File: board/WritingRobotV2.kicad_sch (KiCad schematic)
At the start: 19 parts, among them J1 POWER-INPUT, J2 MOTOR-1-OUTPUT, J3 MOTOR-2-OUTPUT, J4 CAN-INPUT, U1 L7805, U2 MCP2551-I-P

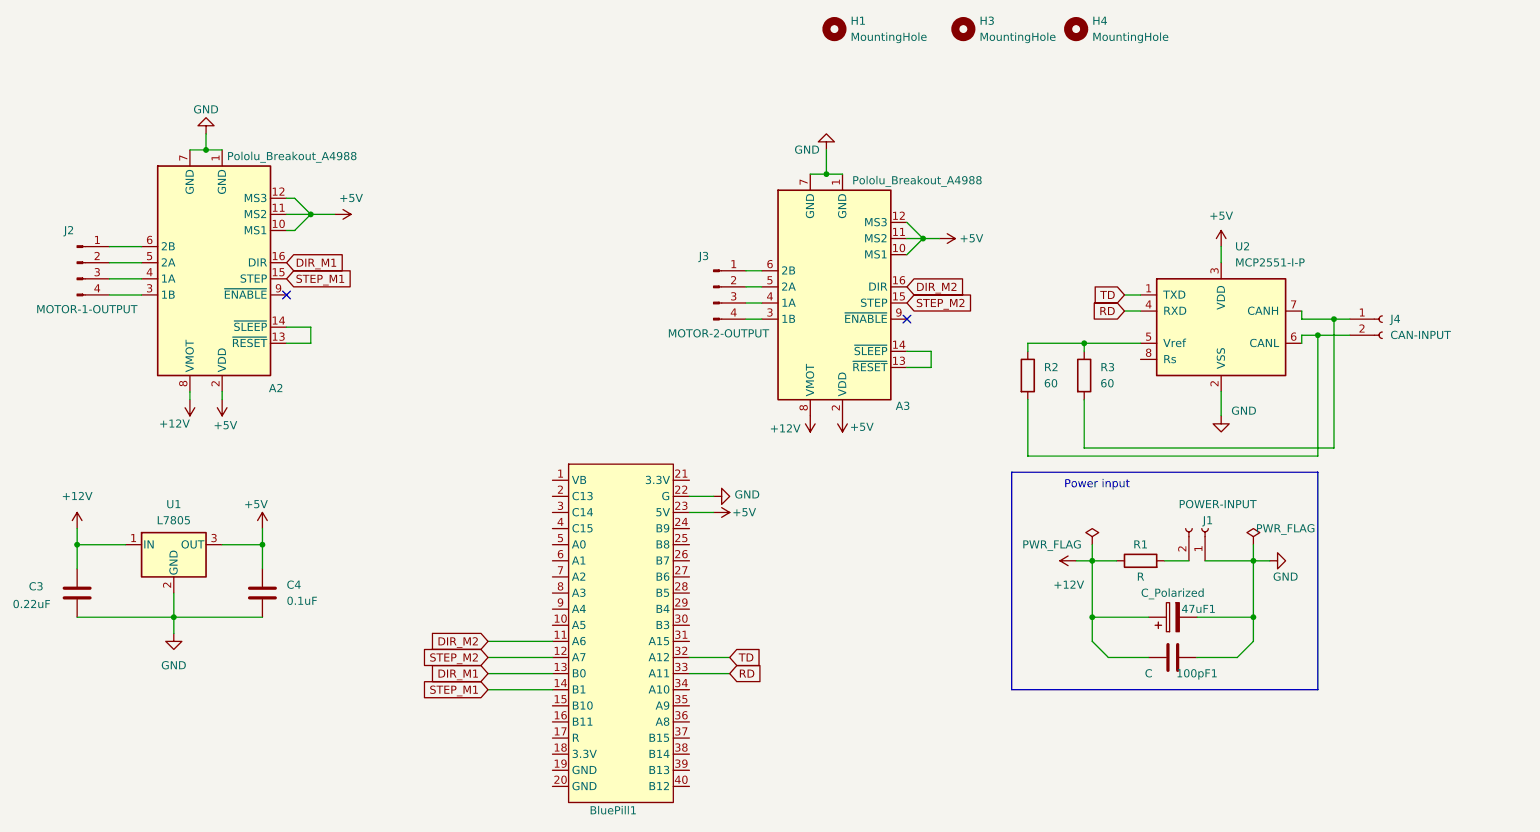
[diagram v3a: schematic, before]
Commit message: Board updated to STM32
Other files in rework
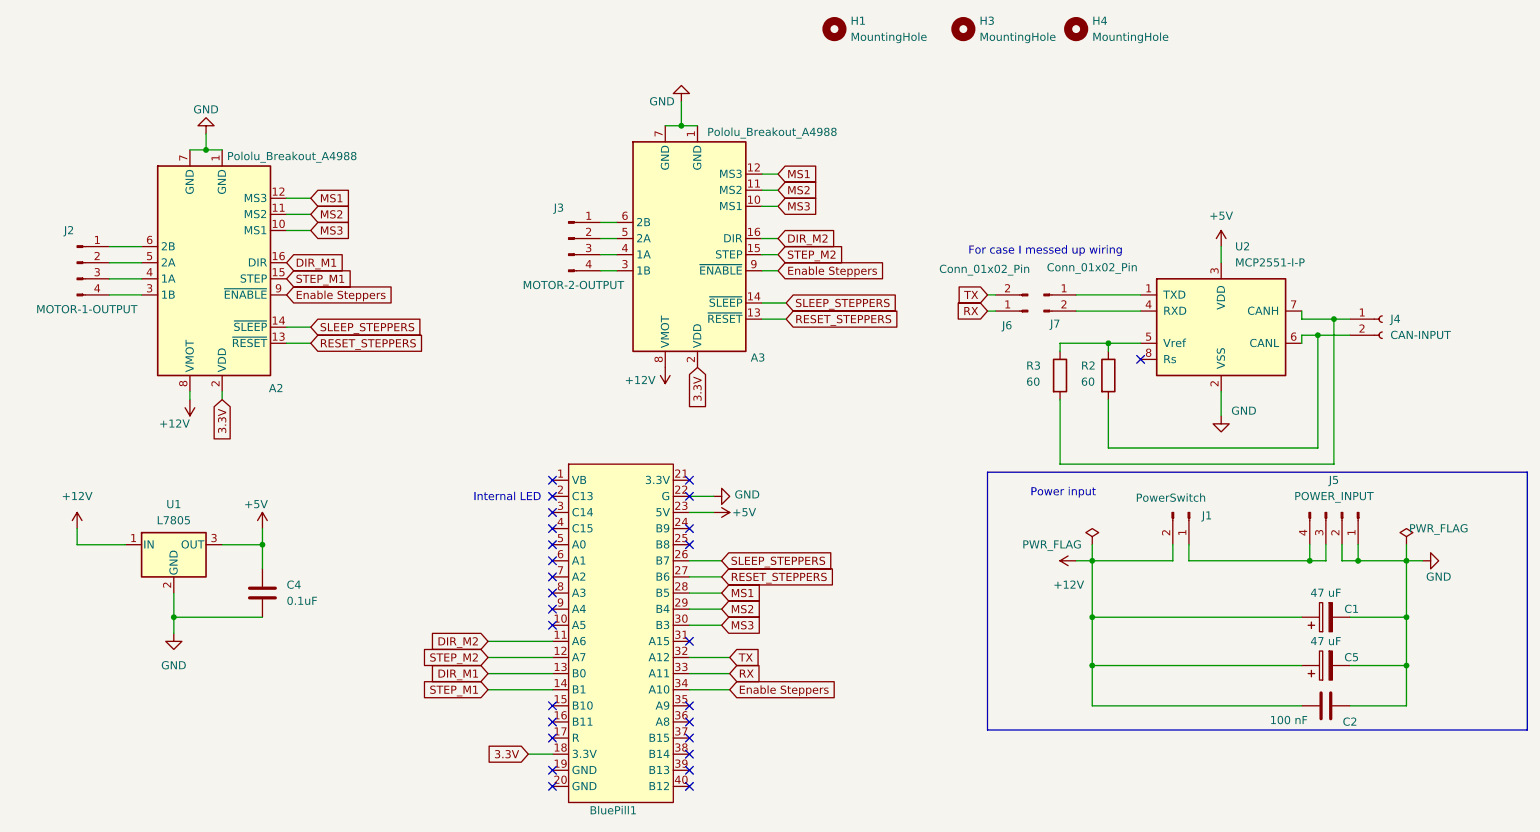
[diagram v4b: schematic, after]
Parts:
- removed C3: 0.22uF, Capacitor_THT:C_Radial_D10.0mm_H16.0mm_P5.00mm, symbol Device:C
- removed J1: POWER-INPUT, Connector_PinSocket_2.54mm:PinSocket_1x02_P2.54mm_Vertical, symbol Connector:Conn_01x02_Socket
- removed R1: R, Resistor_THT:R_Axial_DIN0204_L3.6mm_D1.6mm_P7.62mm_Horizontal, symbol Device:R
- added C5: 47 uF, Capacitor_THT:C_Radial_D8.0mm_H11.5mm_P3.50mm, symbol Device:C_Polarized
- added J1: PowerSwitch, Connector_PinHeader_2.54mm:PinHeader_1x02_P2.54mm_Vertical, symbol Connector:Conn_01x02_Pin
- added J5: POWER_INPUT, Connector_PinHeader_2.54mm:PinHeader_1x04_P2.54mm_Vertical, symbol Connector:Conn_01x04_Pin
- added J6, J7: Conn_01x02_Pin, Connector_PinHeader_2.54mm:PinHeader_1x02_P2.54mm_Vertical, symbol Connector:Conn_01x02_Pin
- C1: renamed from 47uF1; value C_Polarized -> 47 uF; footprint Capacitor_THT:CP_Radial_D5.0mm_P2.50mm -> Capacitor_THT:C_Radial_D8.0mm_H11.5mm_P3.50mm
- C2: renamed from 100pF1; value C -> 100 nF; footprint Capacitor_THT:C_Rect_L4.0mm_W2.5mm_P2.50mm -> Capacitor_THT:C_Disc_D3.0mm_W2.0mm_P2.50mm
- C4: footprint Capacitor_THT:C_Rect_L4.0mm_W2.5mm_P2.50mm -> Capacitor_THT:C_Disc_D3.8mm_W2.6mm_P2.50mm
- U1: footprint Connector_PinHeader_2.54mm:PinHeader_1x03_P2.54mm_Vertical -> Package_TO_SOT_THT:TO-220-3_Vertical
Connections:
- net +12V: now also C5.1, J1.2 (Pin_2)
- net +5V: no longer A2.10 (MS1), A2.11 (MS2), A2.12 (MS3), A2.2 (VDD), A3.10 (MS1), A3.11 (MS2), A3.12 (MS3), A3.2 (VDD)
- net GND: now also C5.2, J5.1 (Pin_1), J5.2 (Pin_2)
- net RESET_STEPPERS: now reaches A3.13 (~{RESET})
- net RESET_STEPPERS: now also A2.13 (~{RESET}), BluePill1.27 (B6); no longer A3.14 (~{SLEEP})
- net Enable Steppers: now reaches A3.9 (~{ENABLE})
- net Enable Steppers: now also A2.9 (~{ENABLE}), BluePill1.34 (A10)
- net 3.3V: now reaches BluePill1.18 (3.3V)
- net 3.3V: now also A2.2 (VDD), A3.2 (VDD)
- net SLEEP_STEPPERS: now reaches BluePill1.26 (B7)
- net SLEEP_STEPPERS: now also A2.14 (~{SLEEP}), A3.14 (~{SLEEP})
- net MS1: now reaches BluePill1.28 (B5)
- net MS1: now also A2.12 (MS3), A3.12 (MS3)
- net MS2: now reaches BluePill1.29 (B4)
- net MS2: now also A2.11 (MS2), A3.11 (MS2)
- net MS3: now reaches BluePill1.30 (B3)
- net MS3: now also A2.10 (MS1), A3.10 (MS1)
- net RD: no longer names the net of U2.4 (RXD)
- net RD: now also J7.2 (Pin_2); no longer BluePill1.33 (A11)
- net TD: no longer names the net of U2.1 (TXD)
- net TD: now also J7.1 (Pin_1); no longer BluePill1.32 (A12)
- new net: J1.1 (Pin_1), J5.3 (Pin_3), J5.4 (Pin_4)
- new net RX: BluePill1.33 (A11), J6.1 (Pin_1)
- new net TX: BluePill1.32 (A12), J6.2 (Pin_2)
- no-connect marks 2 -> 27
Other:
- note added: "For case I messed up wiring"
- note added: "Internal LED"
- moved on the sheet: A3, C1, C2, J3, R2, R3

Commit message: This was send to manufactory
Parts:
- added J10: DEBUG_5V, Connector_PinHeader_2.54mm:PinHeader_1x01_P2.54mm_Vertical, symbol Connector:Conn_01x01_Pin
- added J8: DEBUG_GND, Connector_PinHeader_2.54mm:PinHeader_1x01_P2.54mm_Vertical, symbol Connector:Conn_01x01_Pin
- added J9: DEBUG_12V, Connector_PinHeader_2.54mm:PinHeader_1x01_P2.54mm_Vertical, symbol Connector:Conn_01x01_Pin
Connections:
- net +12V: now also J9.1 (Pin_1)
- net +5V: now also J10.1 (Pin_1)
- net GND: now also J8.1 (Pin_1)
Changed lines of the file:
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@@
 	)
 	(junction
+		(at 255.27 161.29)
+		(diameter 0)
+		(color 0 0 0 0)
+	)
+	(junction
 		(at 66.04 73.66)
 		(diameter 0)
@@
 	)
 	(junction
+		(at 205.74 161.29)
+		(diameter 0)
+		(color 0 0 0 0)
+	)
+	(junction
 		(at 255.27 154.94)
 		(diameter 0)
@@
 	(wire
 		(pts
+			(xy 255.27 161.29) (xy 260.35 161.29)
+		)
+		(stroke
+			(width 0)
+			(type default)
+		)
+	)
+	(wire
+		(pts
 			(xy 66.04 73.66) (xy 68.58 73.66)
 		)
@@
 	(wire
 		(pts
+			(xy 74.93 135.89) (xy 80.01 135.89)
+		)
+		(stroke
+			(width 0)
+			(type default)
+		)
+	)
+	(wire
+		(pts
 			(xy 74.93 133.35) (xy 74.93 135.89)
 		)
@@
 	(wire
 		(pts
+			(xy 200.66 161.29) (xy 205.74 161.29)
+		)
+		(stroke
+			(width 0)
+			(type default)
+		)
+	)
+	(wire
+		(pts
 			(xy 110.49 153.67) (xy 120.65 153.67)
 		)
@@
 	)
 	(symbol
+		(lib_id "Connector:Conn_01x01_Pin")
+		(at 85.09 135.89 180)
+		(unit 1)
+		(exclude_from_sim no)
+		(in_bom yes)
+		(on_board yes)
+		(dnp no)
+		(property "Reference" "J10"
+			(at 84.328 138.684 0)
+			(effects
+				(font
+					(size 1.27 1.27)
+				)
+			)
+		)
+		(property "Value" "DEBUG_5V"
+			(at 84.455 133.35 0)
+			(effects
+				(font
+					(size 1.27 1.27)
+				)
+			)
+		)
+		(property "Footprint" "Connector_PinHeader_2.54mm:PinHeader_1x01_P2.54mm_Vertical"
+			(at 85.09 135.89 0)
+			(effects
+				(font
+					(size 1.27 1.27)
+				)
+				(hide yes)
+			)
+		)
+		(property "Datasheet" "~"
+			(at 85.09 135.89 0)
+			(effects
+				(font
+					(size 1.27 1.27)
+				)
+				(hide yes)
+			)
+		)
+		(property "Description" "Generic connector, single row, 01x01, script generated"
+			(at 85.09 135.89 0)
+			(effects
+				(font
+					(size 1.27 1.27)
+				)
+				(hide yes)
+			)
+		)
+		(pin "1"
+		)
+		(instances
+			(project ""
+				(path "/f0b2f927-a970-450b-9ec6-099adc3d5738"
+					(reference "J10")
+					(unit 1)
+				)
+			)
+		)
+	)
+	(symbol
 		(lib_id "power:+12V")
 		(at 138.43 107.95 180)
@@
 	)
 	(symbol
+		(lib_id "Connector:Conn_01x01_Pin")
+		(at 265.43 161.29 180)
+		(unit 1)
+		(exclude_from_sim no)
+		(in_bom yes)
+		(on_board yes)
+		(dnp no)
+		(property "Reference" "J8"
+			(at 265.176 163.322 0)
+			(effects
+				(font
+					(size 1.27 1.27)
+				)
+			)
+		)
+		(property "Value" "DEBUG_GND"
+			(at 264.795 158.75 0)
+			(effects
+				(font
+					(size 1.27 1.27)
+				)
+			)
+		)
+		(property "Footprint" "Connector_PinHeader_2.54mm:PinHeader_1x01_P2.54mm_Vertical"
+			(at 265.43 161.29 0)
+			(effects
+				(font
+					(size 1.27 1.27)
+				)
+				(hide yes)
+			)
+		)
+		(property "Datasheet" "~"
+			(at 265.43 161.29 0)
+			(effects
+				(font
+					(size 1.27 1.27)
+				)
+				(hide yes)
+			)
+		)
+		(property "Description" "Generic connector, single row, 01x01, script generated"
+			(at 265.43 161.29 0)
+			(effects
+				(font
+					(size 1.27 1.27)
+				)
+				(hide yes)
+			)
+		)
+		(pin "1"
+		)
+		(instances
+			(project ""
+				(path "/f0b2f927-a970-450b-9ec6-099adc3d5738"
+					(reference "J8")
+					(unit 1)
+				)
+			)
+		)
+	)
+	(symbol
 		(lib_id "power:GND")
 		(at 226.06 115.57 0)
@@
 					(unit 1)
 				)
+			)
+		)
+	)
+	(symbol
+		(lib_id "Connector:Conn_01x01_Pin")
+		(at 195.58 161.29 0)
+		(unit 1)
+		(exclude_from_sim no)
+		(in_bom yes)
+		(on_board yes)
+		(dnp no)
+		(property "Reference" "J9"
+			(at 195.326 163.576 0)
+			(effects
+				(font
+					(size 1.27 1.27)
+				)
+			)
+		)
+		(property "Value" "DEBUG_12V"
+			(at 196.596 158.242 0)
+			(effects
+				(font
+					(size 1.27 1.27)
+				)
+			)
+		)
+		(property "Footprint" "Connector_PinHeader_2.54mm:PinHeader_1x01_P2.54mm_Vertical"
+			(at 195.58 161.29 0)
+			(effects
+				(font
+					(size 1.27 1.27)
+				)
+				(hide yes)
+			)
+		)
+		(property "Datasheet" "~"
+			(at 195.58 161.29 0)
+			(effects
+				(font
+					(size 1.27 1.27)
+				)
+				(hide yes)
+			)
+		)
+		(property "Description" "Generic connector, single row, 01x01, script generated"
+			(at 195.58 161.29 0)
+			(effects
+				(font
+					(size 1.27 1.27)
+				)
+				(hide yes)
+			)
+		)
+		(pin "1"
+		)
+		(instances
+			(project ""
+				(path "/f0b2f927-a970-450b-9ec6-099adc3d5738"
+					(reference "J9")
+					(unit 1)
+				)

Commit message: Adding everything
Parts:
- added U3: STM32F103C6Tx, Package_QFP:LQFP-48_7x7mm_P0.5mm, symbol MCU_ST_STM32F1:STM32F103C6Tx
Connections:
- new net: U3.23 (VSS), U3.35 (VSS), U3.47 (VSS)
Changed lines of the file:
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@@
+	)
+	(symbol
+		(lib_id "MCU_ST_STM32F1:STM32F103C6Tx")
+		(at -54.61 182.88 0)
+		(unit 1)
+		(exclude_from_sim no)
+		(in_bom yes)
+		(on_board yes)
+		(dnp no)
+		(fields_autoplaced yes)
+		(property "Reference" "U3"
+			(at -49.8759 220.98 0)
+			(effects
+				(font
+					(size 1.27 1.27)
+				)
+				(justify left)
+			)
+		)
+		(property "Value" "STM32F103C6Tx"
+			(at -49.8759 223.52 0)
+			(effects
+				(font
+					(size 1.27 1.27)
+				)
+				(justify left)
+			)
+		)
+		(property "Footprint" "Package_QFP:LQFP-48_7x7mm_P0.5mm"
+			(at -67.31 218.44 0)
+			(effects
+				(font
+					(size 1.27 1.27)
+				)
+				(justify right)
+				(hide yes)
+			)
+		)
+		(property "Datasheet" "https://www.st.com/resource/en/datasheet/stm32f103c6.pdf"
+			(at -54.61 182.88 0)
+			(effects
+				(font
+					(size 1.27 1.27)
+				)
+				(hide yes)
+			)
+		)
+		(property "Description" "STMicroelectronics Arm Cortex-M3 MCU, 32KB flash, 10KB RAM, 72 MHz, 2.0-3.6V, 37 GPIO, LQFP48"
+			(at -54.61 182.88 0)
+			(effects
+				(font
+					(size 1.27 1.27)
+				)
+				(hide yes)
+			)
+		)
+		(pin "3"
+		)
+		(pin "14"
+		)
+		(pin "10"
+		)
+		(pin "43"
+		)
+		(pin "22"
+		)
+		(pin "18"
+		)
+		(pin "11"
+		)
+		(pin "38"
+		)
+		(pin "17"
+		)
+		(pin "37"
+		)
+		(pin "39"
+		)
+		(pin "21"
+		)
+		(pin "40"
+		)
+		(pin "16"
+		)
+		(pin "7"
+		)
+		(pin "24"
+		)
+		(pin "30"
+		)
+		(pin "46"
+		)
+		(pin "47"
+		)
+		(pin "20"
+		)
+		(pin "33"
+		)
+		(pin "36"
+		)
+		(pin "31"
+		)
+		(pin "15"
+		)
+		(pin "13"
+		)
+		(pin "27"
+		)
+		(pin "29"
+		)
+		(pin "12"
+		)
+		(pin "34"
+		)
+		(pin "41"
+		)
+		(pin "44"
+		)
+		(pin "45"
+		)
+		(pin "5"
+		)
+		(pin "19"
+		)
+		(pin "26"
+		)
+		(pin "9"
+		)
+		(pin "35"
+		)
+		(pin "8"
+		)
+		(pin "1"
+		)
+		(pin "42"
+		)
+		(pin "23"
+		)
+		(pin "48"
+		)
+		(pin "32"
+		)
+		(pin "25"
+		)
+		(pin "28"
+		)
+		(pin "2"
+		)
+		(pin "4"
+		)
+		(pin "6"
+		)
+		(instances
+			(project ""
+				(path "/f0b2f927-a970-450b-9ec6-099adc3d5738"
+					(reference "U3")
+					(unit 1)
+				)
+			)
+		)
 	)
 	(symbol
